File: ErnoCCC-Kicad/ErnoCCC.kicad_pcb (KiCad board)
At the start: 2 copper layers, 161.4 x 95.9 mm, 106 parts, among them J1 6VAC, J2 ICSP, J3 FTDI, J4 Erno Controller, J5 SWITCH, J6 LED OUT, Q1 BC847, Q2 BC847, Q3 BC847, SW1 SW_Push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

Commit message: Gerbers for Rev A
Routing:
- net GND: track 150.8 -> 126.9 mm
- net Net-(Q1-Pad3): track 38.2 -> 43.2 mm
- net (no net): track 0.00 -> 0.85 mm
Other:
- board text added: "JLCJLCJLCJLC"
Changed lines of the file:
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@@
   (general
     (thickness 1.6)
-    (drawings 314)
-    (tracks 1076)
+    (drawings 315)
+    (tracks 1071)
     (zones 0)
     (modules 106)
@@
     (37 F.SilkS user)
     (38 B.Mask user)
-    (39 F.Mask user)
+    (39 F.Mask user hide)
     (40 Dwgs.User user)
     (41 Cmts.User user)
@@
       (viasonmask false)
       (mode 1)
-      (useauxorigin false)
+      (useauxorigin true)
       (hpglpennumber 1)
       (hpglpenspeed 20)
@@
       (outputformat 1)
       (mirror false)
-      (drillshape 1)
+      (drillshape 0)
       (scaleselection 1)
-      (outputdirectory ""))
+      (outputdirectory "/Users/peaceman/code/Arduino/ErnoCCC/ErnoCCC-Kicad/Gerbers-Rev.A/"))
   )
   (net 0 "")
@@
     (tags "Choke SMD")
     (attr smd)
-    (fp_text reference L1 (at -7.239 0 180) (layer F.SilkS)
+    (fp_text reference L1 (at -6.59 2.77 180) (layer F.SilkS)
       (effects (font (size 1 1) (thickness 0.15)))
     )
@@
     )
   )
+  (gr_text JLCJLCJLCJLC (at 223 31.5 90) (layer F.SilkS)
+    (effects (font (size 0.8 0.8) (thickness 0.15)))
+  )
   (gr_arc (start 169.3 91.5) (end 169.3 90.6) (angle -90) (layer Edge.Cuts) (width 0.05))
   (gr_arc (start 209.001361 85.811601) (end 209.6 85.8) (angle -119.3902406) (layer Edge.Cuts) (width 0.05))
@@
   )
   (gr_text LEDs (at 165.354 102.87) (layer F.SilkS)
-    (effects (font (size 1.5 1.5) (thickness 0.3)))
+    (effects (font (size 1.3 1.3) (thickness 0.2)))
   )
-  (gr_text "off  on" (at 167.386 108.458 90) (layer F.SilkS)
+  (gr_text "off  on" (at 167.2 108.458 90) (layer F.SilkS)
     (effects (font (size 1 1) (thickness 0.15)))
   )
@@
   (gr_line (start 97.5 58.587) (end 187.7 58.589) (layer Eco1.User) (width 0.15))
   (gr_line (start 97.5 33.8) (end 97.5 58.587) (layer Eco1.User) (width 0.15))
+  (segment (start 116.8 57.6) (end 116.8 58.44615) (width 0.25) (layer F.Cu) (net 0))
   (segment (start 133.694 94.814696) (end 133.694 97.086) (width 0.25) (layer F.Cu) (net 1))
   (segment (start 133.694 92.592) (end 133.694 94.814696) (width 0.25) (layer F.Cu) (net 1))
@@
   (segment (start 110.6475 54.814) (end 107.678 51.8445) (width 0.25) (layer F.Cu) (net 17))
   (segment (start 107.678 51.8445) (end 107.678 49.226) (width 0.25) (layer F.Cu) (net 17))
-  (segment (start 116.83101 57.87101) (end 116.314 57.354) (width 0.25) (layer F.Cu) (net 17))
-  (segment (start 123.47584 57.87101) (end 116.83101 57.87101) (width 0.25) (layer F.Cu) (net 17))
-  (segment (start 125.33301 56.01384) (end 123.47584 57.87101) (width 0.25) (layer F.Cu) (net 17))
-  (segment (start 125.33301 51.32201) (end 125.33301 56.01384) (width 0.25) (layer F.Cu) (net 17))
-  (segment (start 124.696 50.685) (end 125.33301 51.32201) (width 0.25) (layer F.Cu) (net 17))
   (segment (start 114.3605 58.686) (end 115.6925 57.354) (width 0.25) (layer F.Cu) (net 17))
   (segment (start 114.3605 59.386) (end 114.3605 58.686) (width 0.25) (layer F.Cu) (net 17))
@@
   (segment (start 112.3615 53.1) (end 117.14 53.1) (width 0.25) (layer F.Cu) (net 17))
   (segment (start 110.6475 54.814) (end 112.3615 53.1) (width 0.25) (layer F.Cu) (net 17))
+  (segment (start 124.696 50.685) (end 125.33301 51.32201) (width 0.25) (layer F.Cu) (net 17))
+  (segment (start 123.47584 57.87101) (end 119.917992 57.87101) (width 0.25) (layer F.Cu) (net 17))
+  (segment (start 125.33301 56.01384) (end 123.47584 57.87101) (width 0.25) (layer F.Cu) (net 17))
+  (segment (start 119.917992 57.87101) (end 117.377992 60.41101) (width 0.25) (layer F.Cu) (net 17))
+  (segment (start 115.42299 60.07784) (end 115.42299 58.24501) (width 0.25) (layer F.Cu) (net 17))
+  (segment (start 117.377992 60.41101) (end 115.75616 60.41101) (width 0.25) (layer F.Cu) (net 17))
+  (segment (start 125.33301 51.32201) (end 125.33301 56.01384) (width 0.25) (layer F.Cu) (net 17))
+  (segment (start 115.75616 60.41101) (end 115.42299 60.07784) (width 0.25) (layer F.Cu) (net 17))
+  (segment (start 115.42299 58.24501) (end 116.314 57.354) (width 0.25) (layer F.Cu) (net 17))
   (segment (start 106.728 51.942) (end 108.694 53.908) (width 0.25) (layer F.Cu) (net 18))
   (segment (start 106.728 51.242) (end 106.728 51.942) (width 0.25) (layer F.Cu) (net 18))
@@
   (segment (start 134.498659 91.286659) (end 134.09866 90.88666) (width 0.25) (layer F.Cu) (net 51))
   (segment (start 134.09866 91.447342) (end 134.09866 90.88666) (width 0.25) (layer B.Cu) (net 51))
-  (segment (start 132.48001 72.58499) (end 134.08499 72.58499) (width 0.25) (layer F.Cu) (net 51))
-  (segment (start 131.455 73.61) (end 132.48001 72.58499) (width 0.25) (layer F.Cu) (net 51))
-  (segment (start 130.9675 73.61) (end 131.455 73.61) (width 0.25) (layer F.Cu) (net 51))
-  (segment (start 134.08499 72.58499) (end 135.11 73.61) (width 0.25) (layer F.Cu) (net 51))
-  (segment (start 135.387001 81.348999) (end 135.387001 73.887001) (width 0.25) (layer F.Cu) (net 51))
-  (segment (start 133.694 84.092) (end 133.694 83.042) (width 0.25) (layer F.Cu) (net 51))
-  (segment (start 135.294 80.751002) (end 135.618 80.427002) (width 0.25) (layer F.Cu) (net 51))
-  (segment (start 135.294 84.092) (end 135.294 80.751002) (width 0.25) (layer F.Cu) (net 51))
-  (segment (start 135.618 80.427002) (end 135.618 74.118) (width 0.25) (layer F.Cu) (net 51))
-  (segment (start 135.11 80.935002) (end 135.11 81.738) (width 0.25) (layer F.Cu) (net 51))
-  (segment (start 135.11 81.738) (end 135.387001 81.348999) (width 0.25) (layer F.Cu) (net 51))
-  (segment (start 135.618 80.427002) (end 135.11 80.935002) (width 0.25) (layer F.Cu) (net 51))
-  (segment (start 133.694 83.042) (end 135.11 81.738) (width 0.25) (layer F.Cu) (net 51))
-  (segment (start 126.01101 72.58499) (end 130.02099 72.58499) (width 0.25) (layer F.Cu) (net 51))
-  (segment (start 124.23 74.366) (end 126.01101 72.58499) (width 0.25) (layer F.Cu) (net 51))
-  (segment (start 123.68 74.366) (end 124.23 74.366) (width 0.25) (layer F.Cu) (net 51))
-  (segment (start 130.02099 72.58499) (end 131.046 73.61) (width 0.25) (layer F.Cu) (net 51))
   (via (at 136.126 72.594) (size 0.8) (drill 0.4) (layers F.Cu B.Cu) (net 51))
   (segment (start 136.0475 72.6725) (end 136.126 72.594) (width 0.25) (layer F.Cu) (net 51))
@@
   (segment (start 133.694 84.092) (end 133.694 85.51701) (width 0.25) (layer F.Cu) (net 51))
   (segment (start 133.694 85.51701) (end 133.87699 85.7) (width 0.25) (layer F.Cu) (net 51))
+  (segment (start 133.769001 82.966999) (end 135.029001 82.966999) (width 0.25) (layer F.Cu) (net 51))
+  (segment (start 135.029001 82.966999) (end 135.3 83.237998) (width 0.25) (layer F.Cu) (net 51))
+  (segment (start 133.694 83.042) (end 133.769001 82.966999) (width 0.25) (layer F.Cu) (net 51))
+  (segment (start 133.694 84.092) (end 133.694 83.042) (width 0.25) (layer F.Cu) (net 51))
+  (segment (start 135.387001 80.658001) (end 135.387001 73.987001) (width 0.25) (layer F.Cu) (net 51))
+  (segment (start 135.3 80.745002) (end 135.387001 80.658001) (width 0.25) (layer F.Cu) (net 51))
+  (segment (start 135.3 83.237998) (end 135.3 80.745002) (width 0.25) (layer F.Cu) (net 51))
   (via (at 96.012 64.008) (size 0.8) (drill 0.4) (layers F.Cu B.Cu) (net 52))
   (segment (start 109.7885 59.386) (end 100.634 59.386) (width 0.25) (layer F.Cu) (net 52))

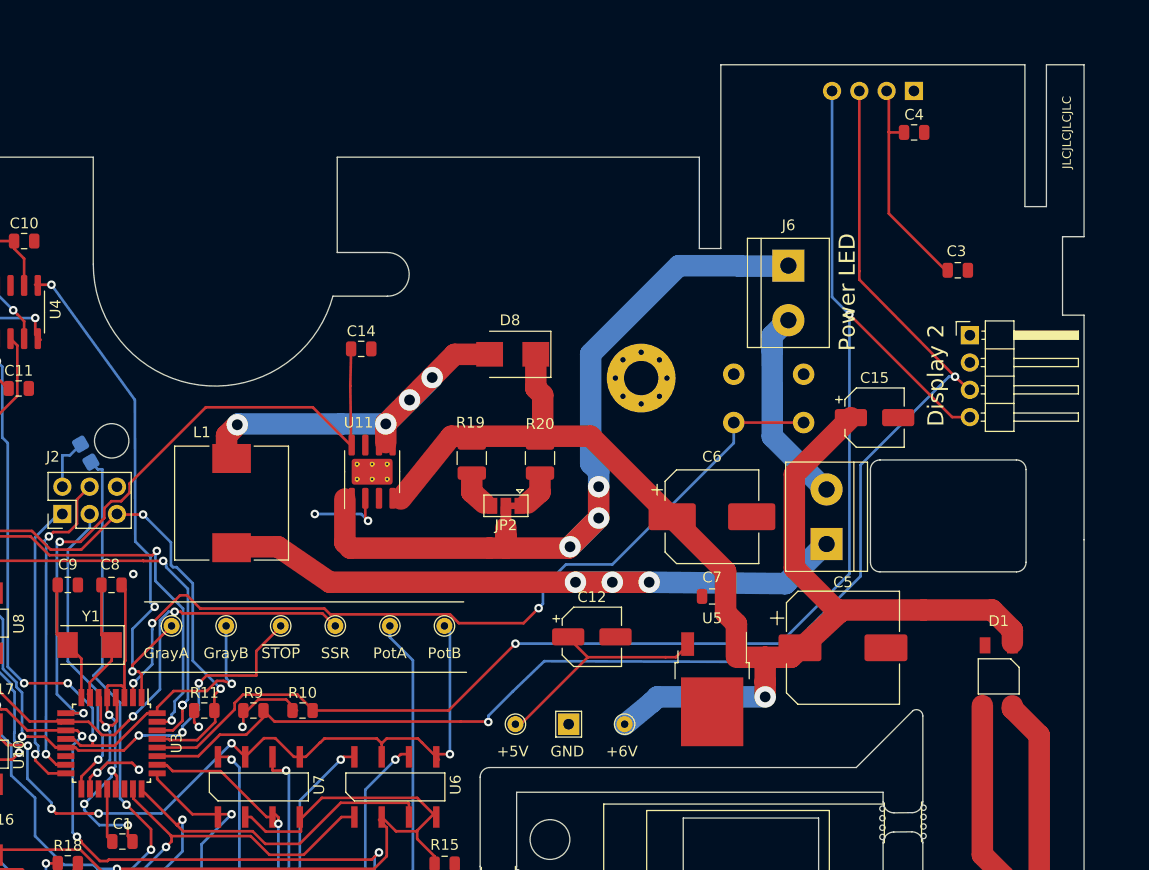
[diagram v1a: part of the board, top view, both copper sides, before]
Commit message: Adding a D10 Breakout for later Vectrol (or MOSFET) experiments
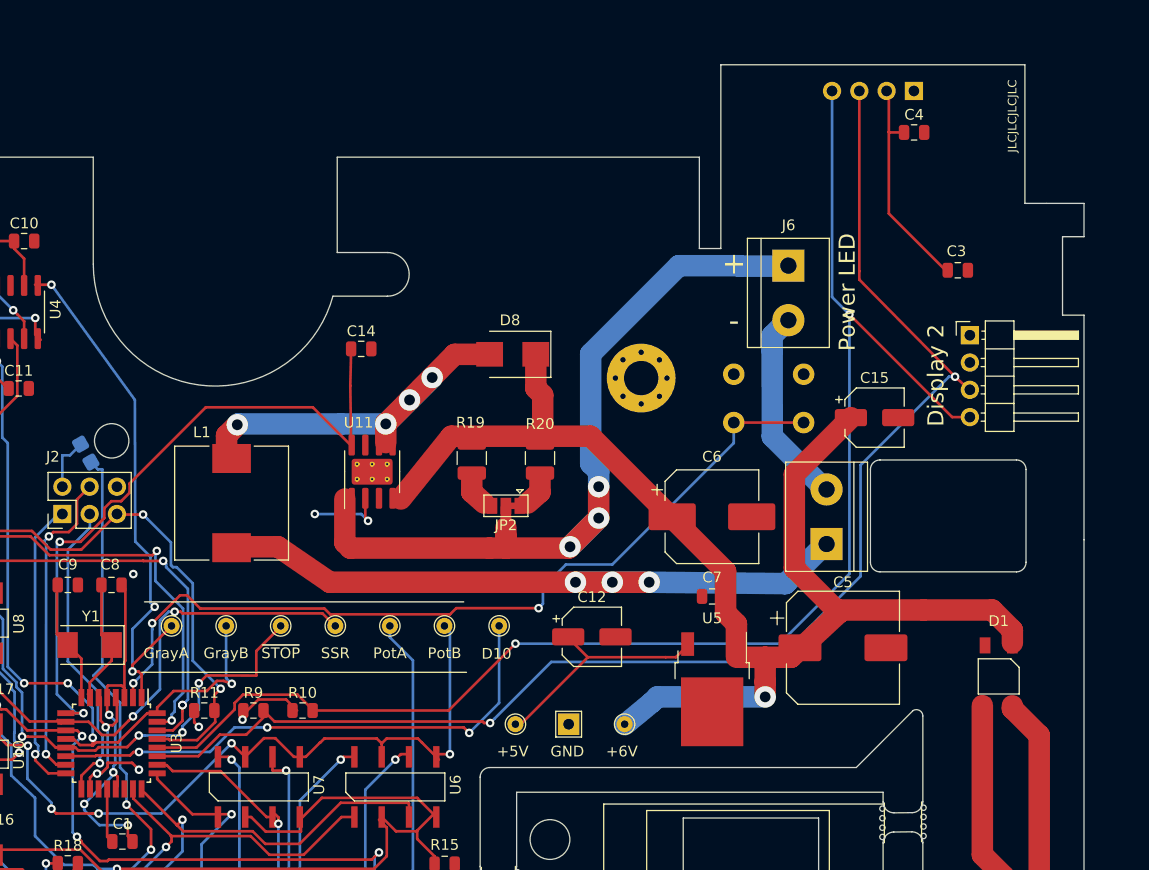
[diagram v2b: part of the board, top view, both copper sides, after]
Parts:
- added TP15: D10, TestPoint:TestPoint_THTPad_D1.5mm_Drill0.7mm, F.Cu at (170.2, 77.4)
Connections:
- U3 pad 14: Net-(U3-Pad14) -> /D10
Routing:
- net /D10: track 0.00 -> 50.0 mm, vias 0 -> 3
- net /BTTN: track 80.4 -> 79.7 mm
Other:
- outline, holes or cut-outs redrawn
- board text added: "+"
- board text added: "-"
- board text added: "D10"

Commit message: Adding TPs to a Header, fixing disconnected GND planes
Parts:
- added J7: Conn_01x07, Connector_PinHeader_2.54mm:PinHeader_1x07_P2.54mm_Horizontal, F.Cu at (213.9, 81.3)
- moved D1 21.9 mm to (221.5, 102.6)
- moved C12 4.07 mm to (181.1, 81.8)
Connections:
- net /ICP1 renamed /GRAY-A
- net /INT1 renamed /GRAY-B
- net Net-(RV1-Pad1) renamed /POTA
- net Net-(TP14-Pad1) renamed /POTB
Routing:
- net /GRAY-B: track 50.5 -> 129.7 mm, vias 3 -> 4
- net /SSR: track 44.6 -> 119.2 mm, vias 2 -> 3
- net /GRAY-A: track 68.0 -> 140.4 mm, vias 5 -> 7
- net /~STOP~: track 47.7 -> 115.1 mm, vias 5 -> 6
- net /D10: track 50.0 -> 113.1 mm, vias 3 -> 5
- net /POTA: track 81.6 -> 142.1 mm, vias 0 -> 2
- net /POTB: track 82.1 -> 139.5 mm
- net GND: track 126.7 -> 163.5 mm, vias 11 -> 12
- net +6V: track 123.6 -> 151.0 mm
- net Net-(D1-Pad4): track 31.4 -> 8.62 mm
- net Net-(D1-Pad3): track 30.6 -> 9.67 mm
- net +5V: track 90.2 -> 108.5 mm, vias 12 -> 13
- net /SCL: track 133.5 -> 128.8 mm, vias 2 -> 3
- net /LED-Net2: track 74.3 -> 73.1 mm
- net /LED-Net4: track 64.5 -> 65.6 mm
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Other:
- board text added: "ICSP"

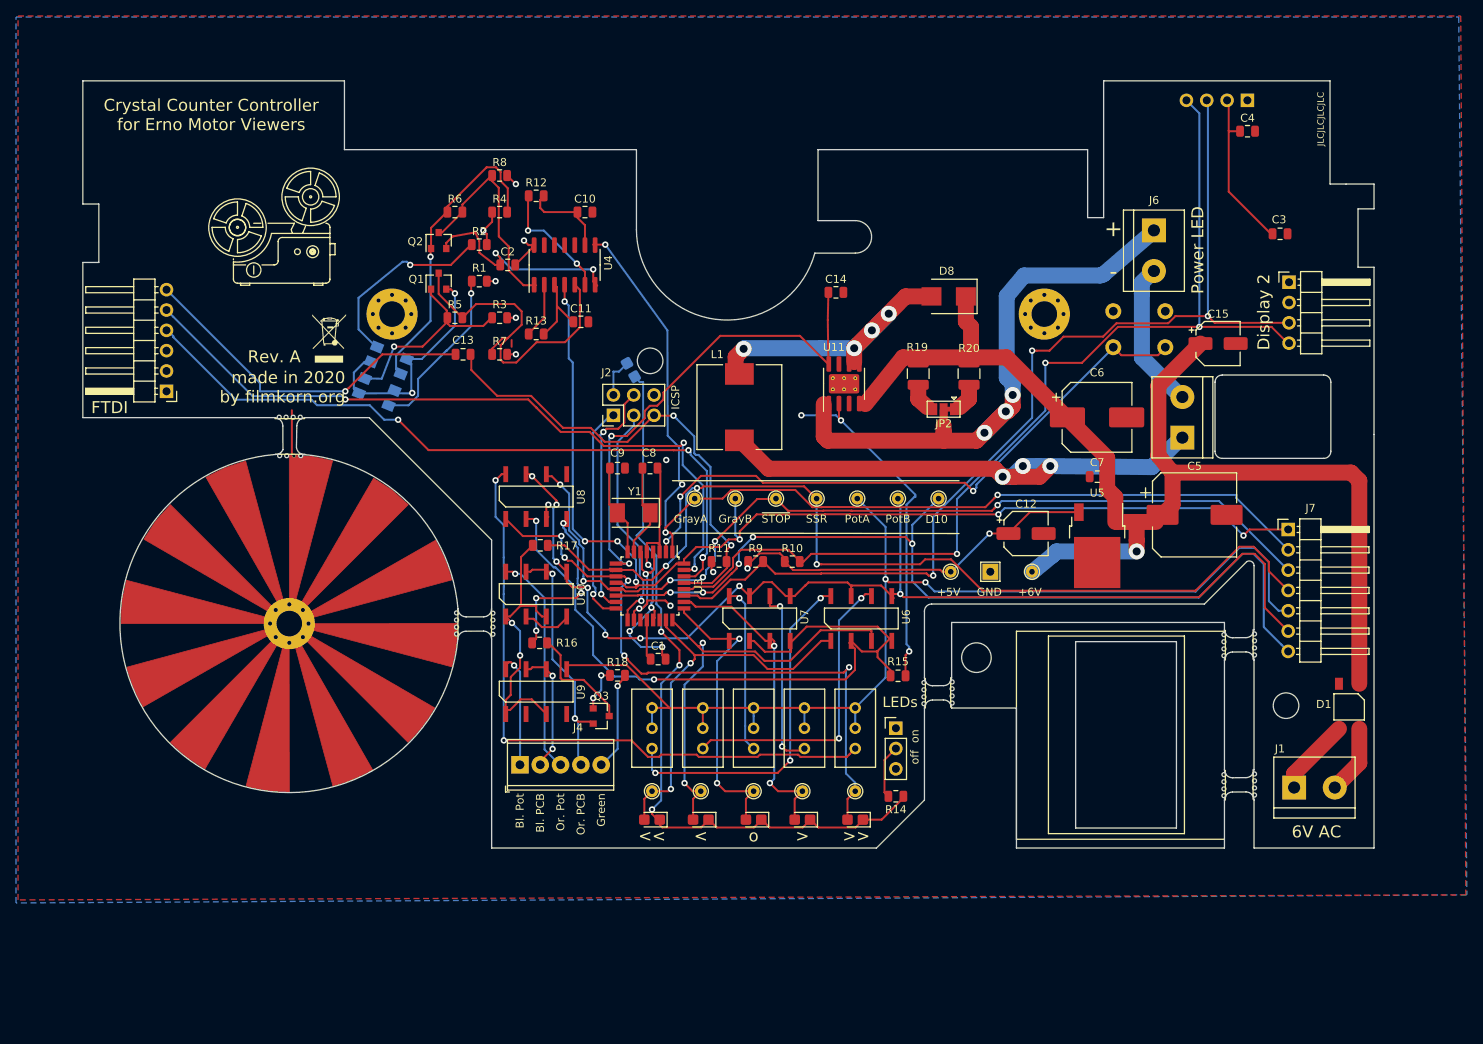
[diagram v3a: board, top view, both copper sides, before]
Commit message: Updating to bigger (and curved) MouseBites to match JLCPCB's DRCs
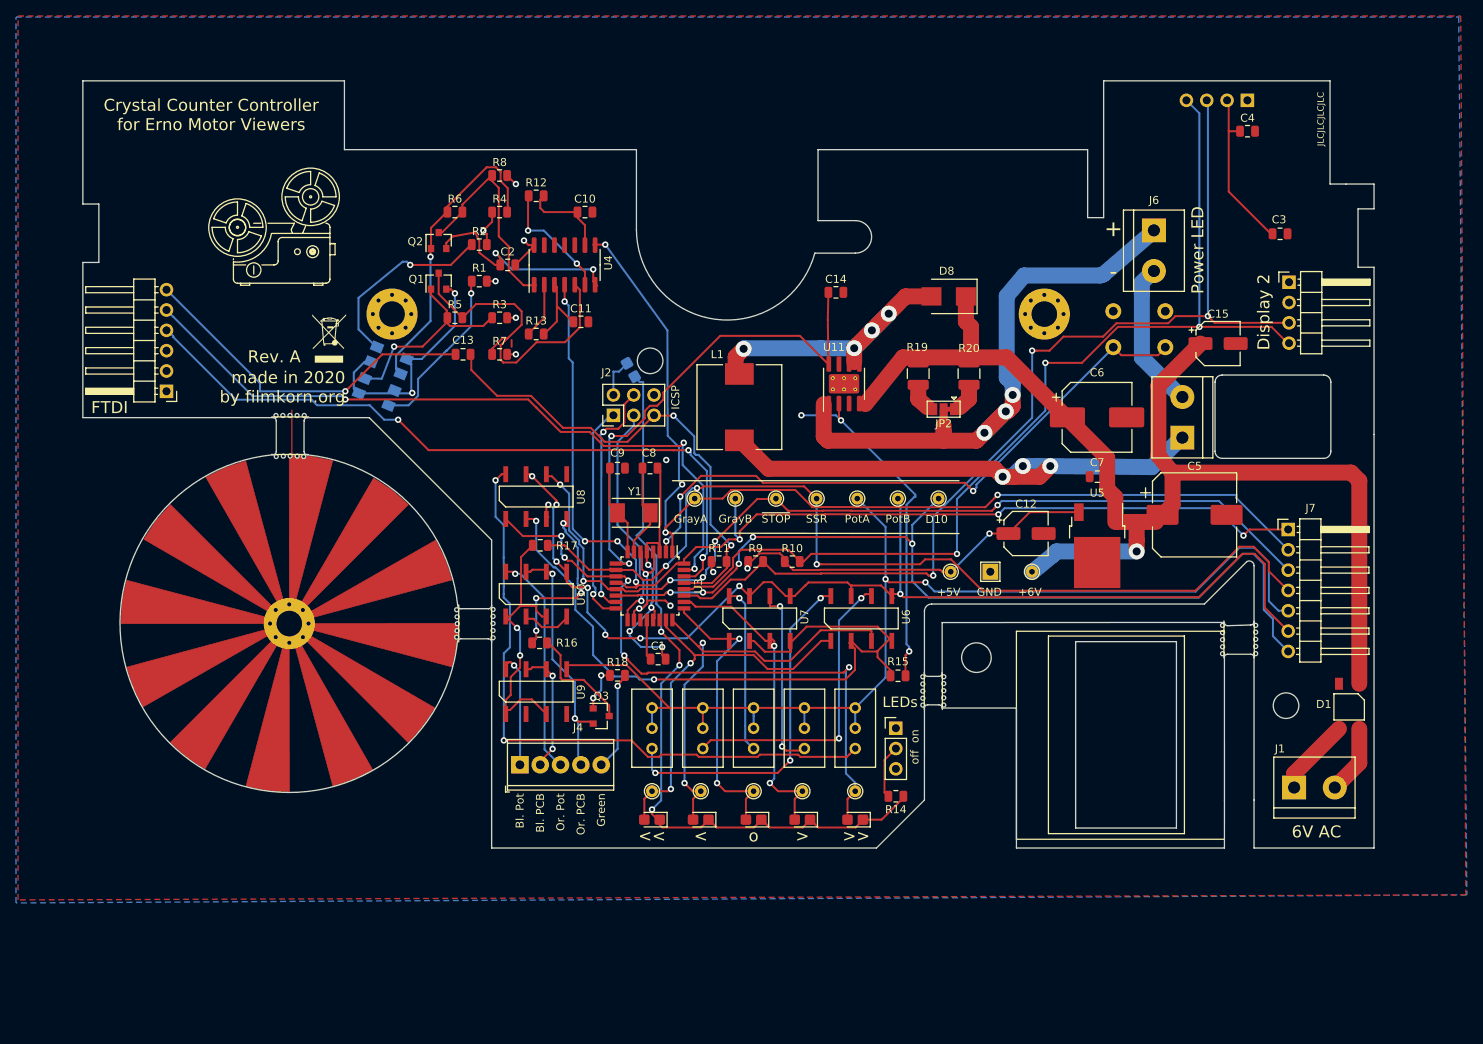
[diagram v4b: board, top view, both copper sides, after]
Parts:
- removed the REF** at (111.9, 93.0)
- removed the REF** at (89.0, 69.2)
- removed the REF** at (207.7, 95.6)
- removed the REF** at (207.8, 95.8)
- removed the REF** at (169.9, 101.6)
- removed the REF** at (170.3, 101.8)
- removed the REF** at (207.8, 113.3)
- removed the REF** at (207.7, 113.1)
- removed the REF** at (89.1, 70.1)
- added REF**: Mouse Bites 4x1, ErnoCCC:MouseBites5x1, F.Cu at (89.1, 68.9)
- added REF**: Mouse Bites 4x1, ErnoCCC:MouseBites5x1_curved, F.Cu at (89.1, 70.6)
- added REF**: Mouse Bites 4x1, ErnoCCC:MouseBites5x1_curved, F.Cu at (111.5, 93.0)
- added REF**: Mouse Bites 4x1, ErnoCCC:MouseBites5x1, F.Cu at (207.9, 95.0)
- added REF**: Mouse Bites 4x1, ErnoCCC:MouseBites5x1, F.Cu at (207.5, 95.0)
- added REF**: Mouse Bites 4x1, ErnoCCC:MouseBites5x1, F.Cu at (168.9, 101.4)
- added REF**: Mouse Bites 4x1, ErnoCCC:MouseBites5x1, F.Cu at (170.1, 101.5)
- REF**: footprint ErnoCCC:MouseBites4x1 -> ErnoCCC:MouseBites5x1
- moved REF** 0.09 mm to (112.6, 93.0)
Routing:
- net Net-(RV5-Pad3): track 80.2 -> 80.8 mm
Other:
- outline, holes or cut-outs redrawn
